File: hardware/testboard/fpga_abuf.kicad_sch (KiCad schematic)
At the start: 11 parts, among them U14 SN74ALVC164245, U15 SN74ALVC164245

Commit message: simpleboard nearly complete
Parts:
- removed R19: R_Small_US, symbol Device:R_Small_US
- C32, C33, C34, C35, C36, C37, C38, C39: footprint (none) -> Capacitor_SMD:C_0603_1608Metric
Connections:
- net FPGA_ABUF_DIR is gone; now on net GND: U14.1 (1DIR), U14.24 (2DIR), U15.1 (1DIR), U15.24 (2DIR)
- net FPGA_ABUF_~{OE} is gone; now on net GND: U14.25 (*2OE), U14.48 (*1OE), U15.25 (*2OE), U15.48 (*1OE)

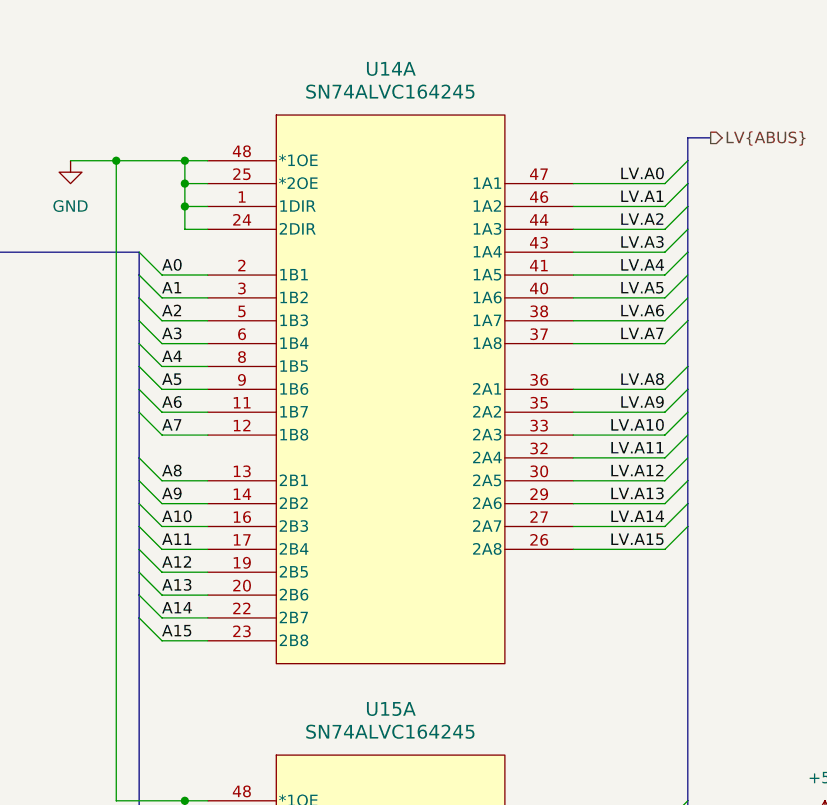
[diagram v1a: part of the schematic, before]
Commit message: fix up FPGA pinning
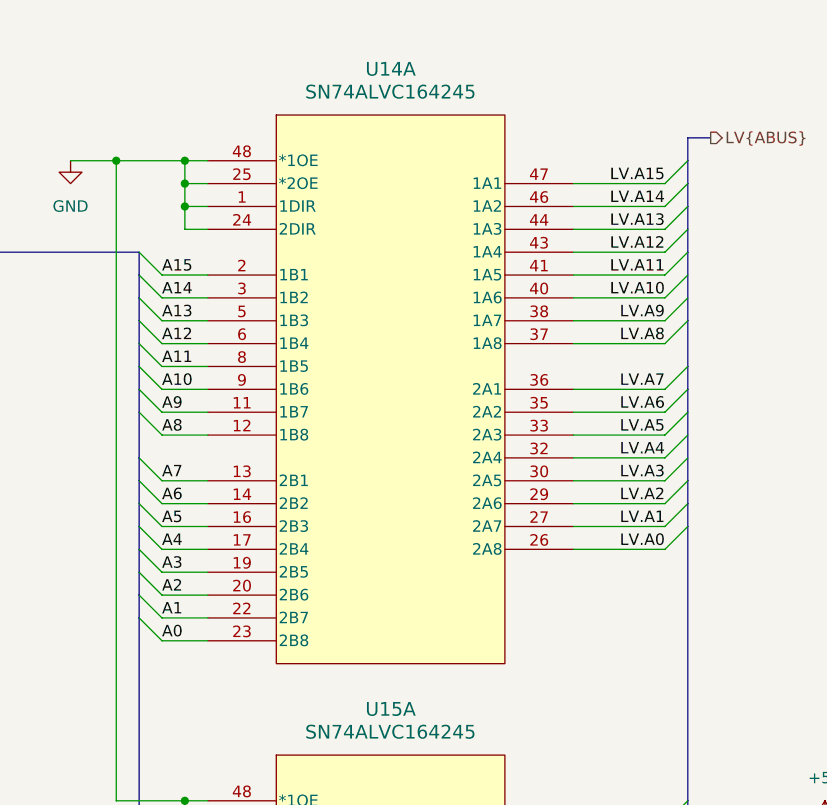
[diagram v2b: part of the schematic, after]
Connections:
- net A0: now also U14.23 (2B8); no longer U14.2 (1B1)
- net A1: now also U14.22 (2B7); no longer U14.3 (1B2)
- net A10: now also U14.9 (1B6); no longer U14.16 (2B3)
- net A11: now also U14.8 (1B5); no longer U14.17 (2B4)
- net A12: now also U14.6 (1B4); no longer U14.19 (2B5)
- net A13: now also U14.5 (1B3); no longer U14.20 (2B6)
- net A14: now also U14.3 (1B2); no longer U14.22 (2B7)
- net A15: now also U14.2 (1B1); no longer U14.23 (2B8)
- net A2: now also U14.20 (2B6); no longer U14.5 (1B3)
- net A3: now also U14.19 (2B5); no longer U14.6 (1B4)
- net A4: now also U14.17 (2B4); no longer U14.8 (1B5)
- net A5: now also U14.16 (2B3); no longer U14.9 (1B6)
- net A6: now also U14.14 (2B2); no longer U14.11 (1B7)
- net A7: now also U14.13 (2B1); no longer U14.12 (1B8)
- net A8: now also U14.12 (1B8); no longer U14.13 (2B1)
- net A9: now also U14.11 (1B7); no longer U14.14 (2B2)
- net LV.A0: now also U14.26 (2A8); no longer U14.47 (1A1)
- net LV.A1: now also U14.27 (2A7); no longer U14.46 (1A2)
- net LV.A10: now also U14.40 (1A6); no longer U14.33 (2A3)
- net LV.A11: now also U14.41 (1A5); no longer U14.32 (2A4)
- net LV.A12: now also U14.43 (1A4); no longer U14.30 (2A5)
- net LV.A13: now also U14.44 (1A3); no longer U14.29 (2A6)
- net LV.A14: now also U14.46 (1A2); no longer U14.27 (2A7)
- net LV.A15: now also U14.47 (1A1); no longer U14.26 (2A8)
- net LV.A2: now also U14.29 (2A6); no longer U14.44 (1A3)
- net LV.A3: now also U14.30 (2A5); no longer U14.43 (1A4)
- net LV.A4: now also U14.32 (2A4); no longer U14.41 (1A5)
- net LV.A5: now also U14.33 (2A3); no longer U14.40 (1A6)
- net LV.A6: now also U14.35 (2A2); no longer U14.38 (1A7)
- net LV.A7: now also U14.36 (2A1); no longer U14.37 (1A8)
- net LV.A8: now also U14.37 (1A8); no longer U14.36 (2A1)
- net LV.A9: now also U14.38 (1A7); no longer U14.35 (2A2)
